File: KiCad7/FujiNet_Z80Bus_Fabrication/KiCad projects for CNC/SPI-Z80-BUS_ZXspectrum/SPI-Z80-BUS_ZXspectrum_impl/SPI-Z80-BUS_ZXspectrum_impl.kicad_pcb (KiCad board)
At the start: 2 copper layers, 155 x 55 mm, 29 parts, among them IC1 74HC32N, J1 PinHeader_2.54mm, J2 LOCAL_D, J3 ESP_SPI_INT, J4 ESP_CONTROL, J5 Z80_CONTROL, J6 LOCAL_A-L, J7 LOCAL_A-H

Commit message: Fabrication updates (gcode)
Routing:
- net /SPI-Z80-BUS/LOCAL_D6: track 45.4 -> 32.2 mm, vias 0 -> 2
- net GND: track 301.4 -> 313.7 mm, vias 5 -> 10
- net +5V: track 303.1 -> 311.5 mm, vias 6 -> 9
- net /SPI-Z80-BUS/ESP_SPI_INT.CE: track 162.2 -> 169.1 mm, vias 0 -> 3
- net /SPI-Z80-BUS/ESP_CONTROL.WR: track 127.9 -> 134.5 mm, vias 1 -> 4
- net Net-(ESP_CONTROL.WR1-SER): track 28.6 -> 33.5 mm, vias 0 -> 2
- net /SPI-Z80-BUS/ESP_CONTROL.BUSRQ: track 77.2 -> 82.1 mm, vias 1 -> 5
- net /SPI-Z80-BUS/ESP_SPI_INT.SCK: track 270.0 -> 274.9 mm, vias 4 -> 8
- net /SPI-Z80-BUS/ESP_SPI_INT.STC: track 170.9 -> 175.0 mm, vias 2 -> 5
- net /SPI-Z80-BUS/LOCAL_A0: track 40.7 -> 44.3 mm, vias 1 -> 3
- net Net-(LOCAL_A-L.RD1-DS): track 54.9 -> 58.4 mm
- net /SPI-Z80-BUS/ESP_SPI_INT.OE: track 185.6 -> 189.0 mm
- net /SPI-Z80-BUS/LOCAL_A1: track 30.9 -> 33.9 mm, vias 0 -> 2
- net /SPI-Z80-BUS/ESP_CONTROL.ROMCS: track 54.9 -> 57.8 mm, vias 1 -> 2
- net /SPI-Z80-BUS/LOCAL_CONTROL.MEMRQ: track 82.2 -> 85.1 mm, vias 1 -> 3
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
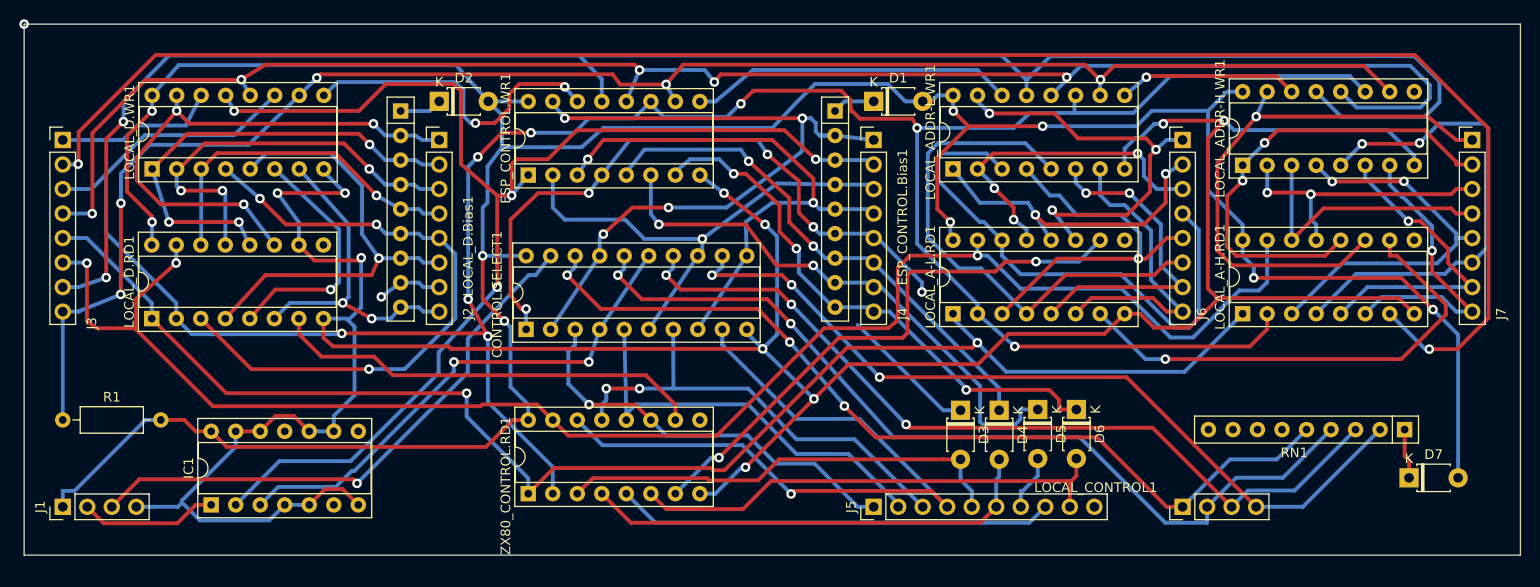
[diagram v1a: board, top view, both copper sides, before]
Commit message: KiCad SPI fixed
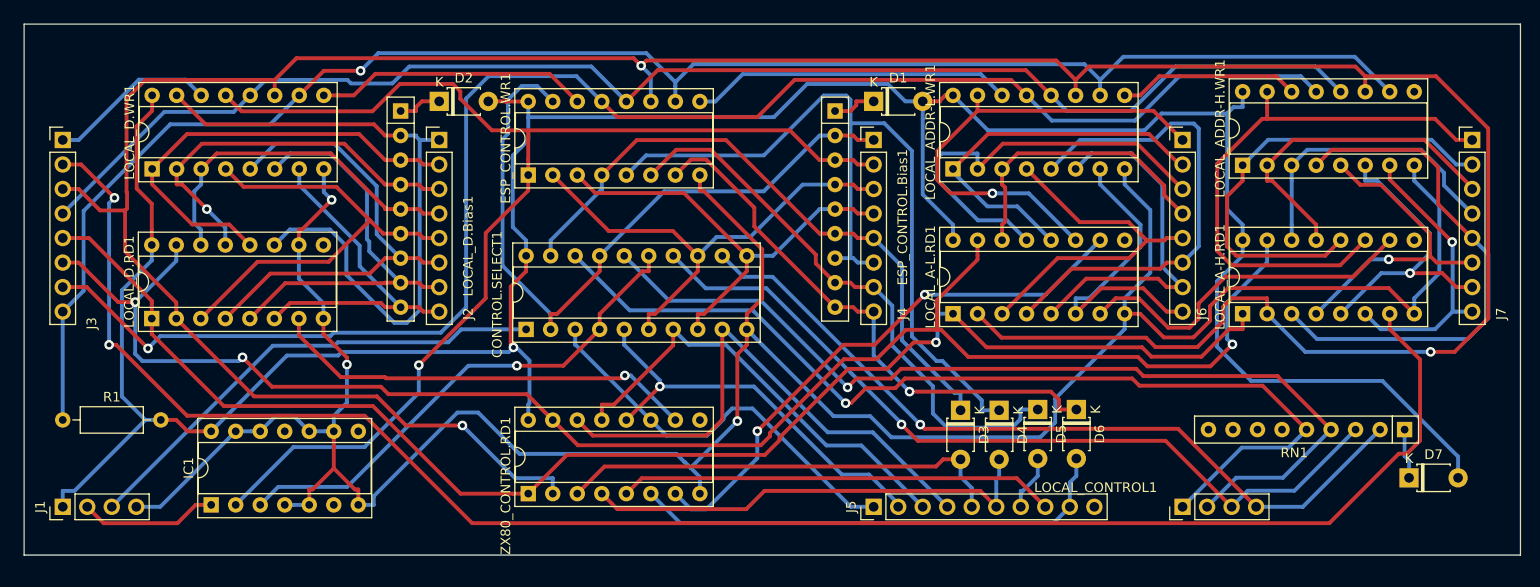
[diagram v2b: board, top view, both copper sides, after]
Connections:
- CONTROL.SELECT1 pad 1: /SPI-Z80-BUS/ESP_CONTROL.BUSRQ -> /SPI-Z80-BUS/!ESP_HARDLOCK
- CONTROL.SELECT1 pad 19: /SPI-Z80-BUS/!ESP_HARDLOCK -> /SPI-Z80-BUS/ESP_CONTROL.BUSRQ
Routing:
- net /SPI-Z80-BUS/ESP_SPI_INT.SCK: track 274.9 -> 317.9 mm, vias 8 -> 3
- net GND: track 313.7 -> 275.2 mm, vias 10 -> 3
- net /SPI-Z80-BUS/ESP_CONTROL.WAIT: track 54.1 -> 87.0 mm, vias 2 -> 0
- net /SPI-Z80-BUS/ESP_SPI_INT.STC: track 175.0 -> 146.6 mm, vias 5 -> 0
- net /SPI-Z80-BUS/LOCAL_A3: track 56.1 -> 30.2 mm
- net +5V: track 311.5 -> 286.8 mm, vias 9 -> 1
- net /SPI-Z80-BUS/ESP_SPI_INT.OE: track 189.0 -> 164.5 mm, vias 2 -> 1
- net /SPI-Z80-BUS/LOCAL_D4: track 64.7 -> 46.8 mm, vias 3 -> 0
- net /SPI-Z80-BUS/Z80_CONTROL.MEMRQ: track 74.2 -> 56.6 mm, vias 1 -> 0
- net /SPI-Z80-BUS/LOCAL_A13: track 50.2 -> 33.4 mm, vias 2 -> 1
- net /SPI-Z80-BUS/ESP_CONTROL.BUSRQ: track 82.1 -> 66.4 mm, vias 5 -> 0
- net /SPI-Z80-BUS/LOCAL_A12: track 40.3 -> 54.2 mm, vias 2 -> 0
- net Net-(LOCAL_A-H.RD1-DS): track 50.2 -> 36.6 mm, vias 1 -> 0
- net /SPI-Z80-BUS/LOCAL_D0: track 56.0 -> 68.8 mm, vias 3 -> 0
- net /SPI-Z80-BUS/LOCAL_D6: track 32.2 -> 44.2 mm, vias 2 -> 0
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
